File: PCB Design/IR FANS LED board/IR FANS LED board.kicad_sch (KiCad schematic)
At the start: 9 parts

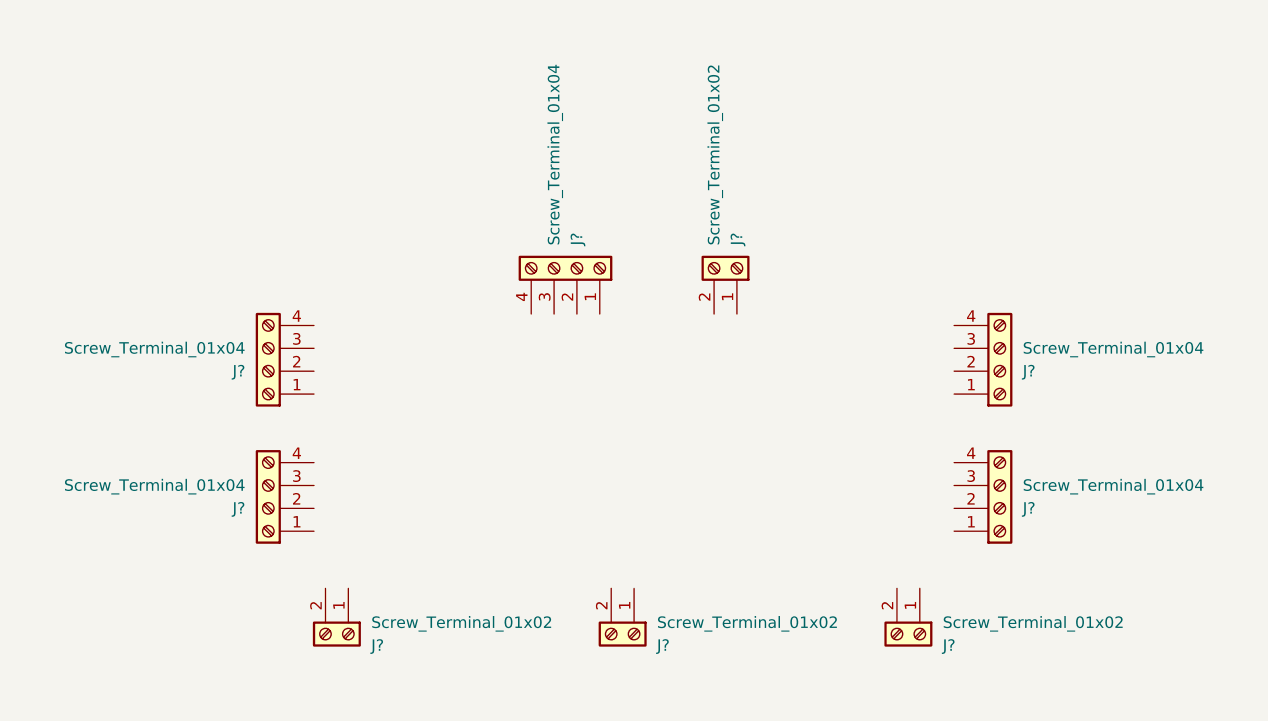
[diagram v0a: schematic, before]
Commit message: schematic now has no errors
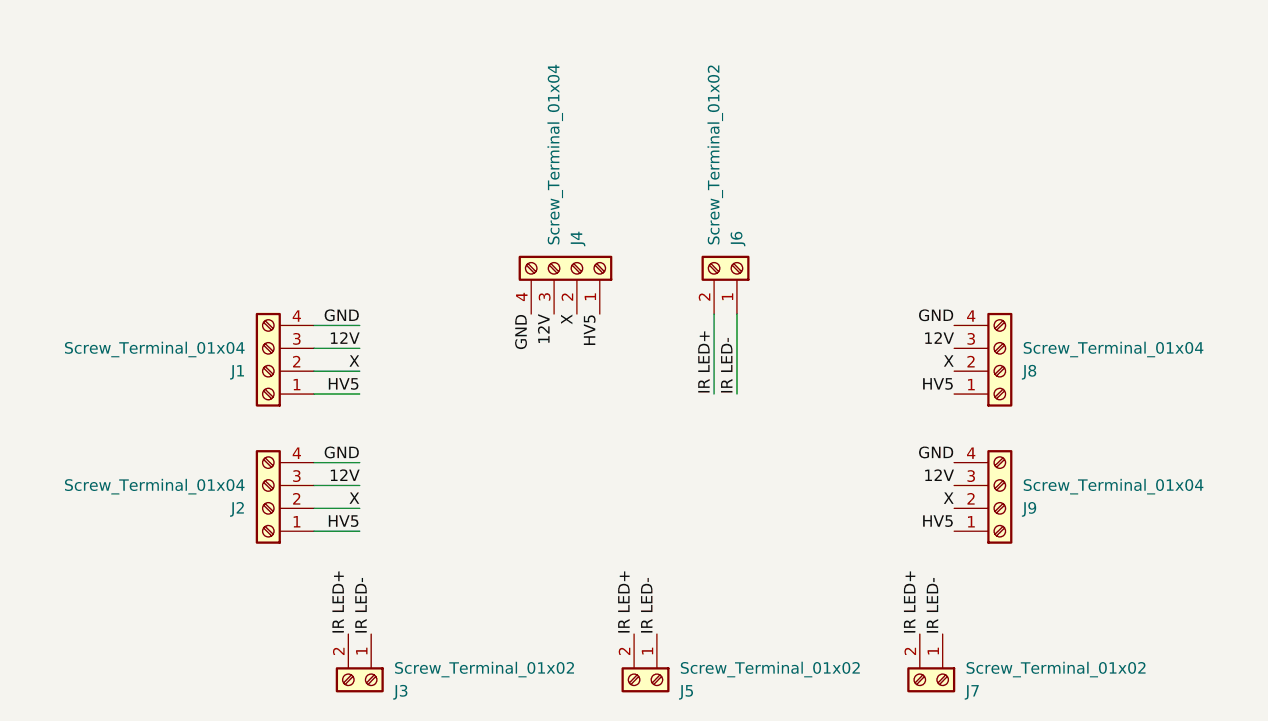
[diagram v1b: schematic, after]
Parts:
- gave numbers to parts that had none: 9
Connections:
- net HV5: now reaches J2.1 (Pin_1)
- net HV5: now also J1.1 (Pin_1), J4.1 (Pin_1), J8.1 (Pin_1), J9.1 (Pin_1)
- net X: now reaches J2.2 (Pin_2)
- net X: now also J1.2 (Pin_2), J4.2 (Pin_2), J8.2 (Pin_2), J9.2 (Pin_2)
- net 12V: now reaches J2.3 (Pin_3)
- net 12V: now also J1.3 (Pin_3), J4.3 (Pin_3), J8.3 (Pin_3), J9.3 (Pin_3)
- net GND: now reaches J2.4 (Pin_4)
- net GND: now also J1.4 (Pin_4), J4.4 (Pin_4), J8.4 (Pin_4), J9.4 (Pin_4)
- net IR LED-: now reaches J7.1 (Pin_1)
- net IR LED-: now also J3.1 (Pin_1), J5.1 (Pin_1), J6.1 (Pin_1)
- net IR LED+: now reaches J7.2 (Pin_2)
- net IR LED+: now also J3.2 (Pin_2), J5.2 (Pin_2), J6.2 (Pin_2)
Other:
- moved on the sheet: J3, J5, J7

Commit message: Labeling on components
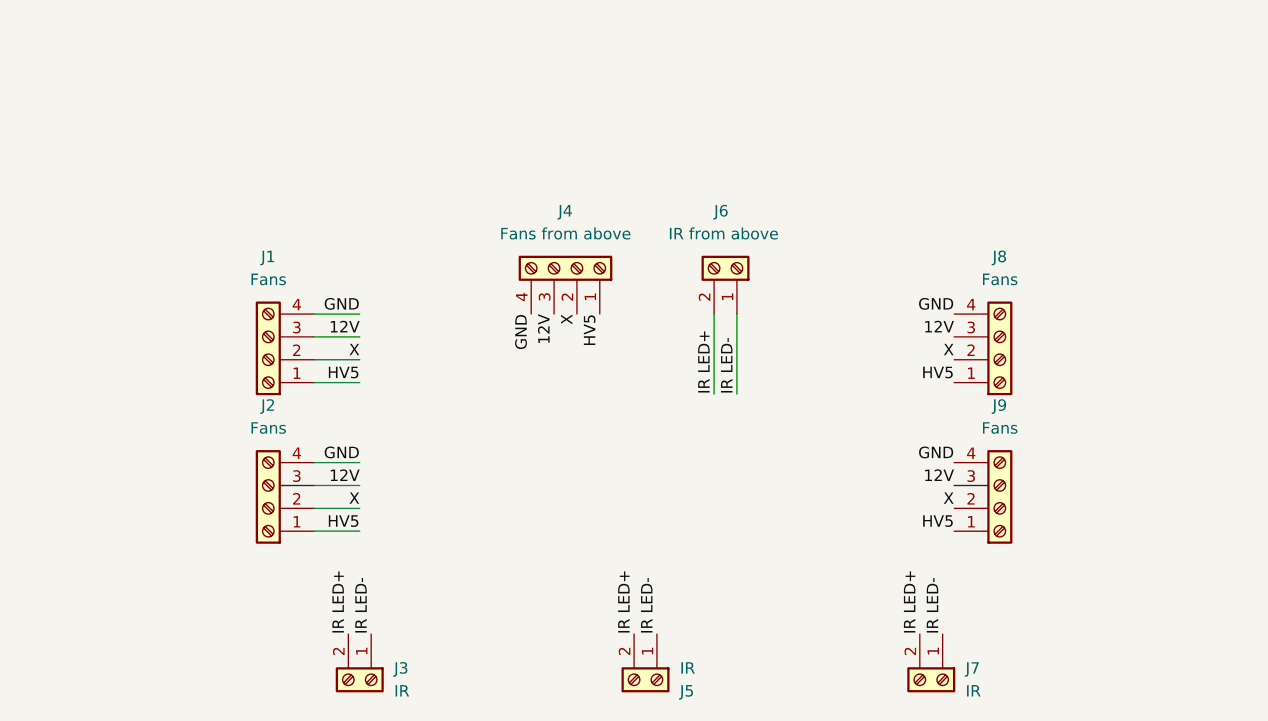
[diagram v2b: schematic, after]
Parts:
- J1, J2, J8, J9: value Screw_Terminal_01x04 -> Fans
- J3, J5, J7: value Screw_Terminal_01x02 -> IR
- J4: value Screw_Terminal_01x04 -> Fans from above
- J6: value Screw_Terminal_01x02 -> IR from above
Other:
- moved on the sheet: J1, J8

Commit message: V2 IR and RGW boards done
Main board missing button footprint
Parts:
- J3, J5, J6, J7: footprint Connector_PinHeader_2.54mm:PinHeader_1x02_P2.54mm_Vertical -> TerminalBlock:TerminalBlock_bornier-2_P5.08mm
- J4: footprint Connector_PinHeader_2.54mm:PinHeader_1x04_P2.54mm_Vertical -> TerminalBlock:TerminalBlock_bornier-4_P5.08mm
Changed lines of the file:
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@@
       (effects (font (size 1.27 1.27)) (justify left))
     )
-    (property "Footprint" "Connector_PinHeader_2.54mm:PinHeader_1x02_P2.54mm_Vertical" (id 2) (at 133.35 106.68 0)
+    (property "Footprint" "TerminalBlock:TerminalBlock_bornier-2_P5.08mm" (id 2) (at 133.35 106.68 0)
       (effects (font (size 1.27 1.27)) hide)
     )
@@
       (effects (font (size 1.27 1.27)) (justify left))
     )
-    (property "Footprint" "Connector_PinHeader_2.54mm:PinHeader_1x02_P2.54mm_Vertical" (id 2) (at 69.85 106.68 0)
+    (property "Footprint" "TerminalBlock:TerminalBlock_bornier-2_P5.08mm" (id 2) (at 69.85 106.68 0)
       (effects (font (size 1.27 1.27)) hide)
     )
@@
       (effects (font (size 1.27 1.27)) (justify left))
     )
-    (property "Footprint" "Connector_PinHeader_2.54mm:PinHeader_1x02_P2.54mm_Vertical" (id 2) (at 110.49 60.96 0)
+    (property "Footprint" "TerminalBlock:TerminalBlock_bornier-2_P5.08mm" (id 2) (at 110.49 60.96 0)
       (effects (font (size 1.27 1.27)) hide)
     )
@@
       (effects (font (size 1.27 1.27)) (justify left))
     )
-    (property "Footprint" "Connector_PinHeader_2.54mm:PinHeader_1x02_P2.54mm_Vertical" (id 2) (at 101.6 106.68 0)
+    (property "Footprint" "TerminalBlock:TerminalBlock_bornier-2_P5.08mm" (id 2) (at 101.6 106.68 0)
       (effects (font (size 1.27 1.27)) hide)
     )
@@
     (property "Reference" "J4" (id 0) (at 91.44 54.61 90))
     (property "Value" "Fans from above" (id 1) (at 91.44 57.15 90))
-    (property "Footprint" "Connector_PinHeader_2.54mm:PinHeader_1x04_P2.54mm_Vertical" (id 2) (at 92.71 60.96 0)
+    (property "Footprint" "TerminalBlock:TerminalBlock_bornier-4_P5.08mm" (id 2) (at 92.71 60.96 0)
       (effects (font (size 1.27 1.27)) hide)
     )
@@
     )
     (path "/609e8a66-54cb-40fe-9889-7eaa62dba117"
-      (reference "J3") (unit 1) (value "IR") (footprint "Connector_PinHeader_2.54mm:PinHeader_1x02_P2.54mm_Vertical")
+      (reference "J3") (unit 1) (value "IR") (footprint "TerminalBlock:TerminalBlock_bornier-2_P5.08mm")
     )
     (path "/fd479909-e292-4092-97ac-01b2689407fd"
-      (reference "J4") (unit 1) (value "Fans from above") (footprint "Connector_PinHeader_2.54mm:PinHeader_1x04_P2.54mm_Vertical")
+      (reference "J4") (unit 1) (value "Fans from above") (footprint "TerminalBlock:TerminalBlock_bornier-4_P5.08mm")
     )
     (path "/b58268f9-87ea-4c46-ab23-f79565efd06e"
-      (reference "J5") (unit 1) (value "IR") (footprint "Connector_PinHeader_2.54mm:PinHeader_1x02_P2.54mm_Vertical")
+      (reference "J5") (unit 1) (value "IR") (footprint "TerminalBlock:TerminalBlock_bornier-2_P5.08mm")
     )
     (path "/88f10c66-dda7-46b8-8caf-c98ed0e09c27"
-      (reference "J6") (unit 1) (value "IR from above") (footprint "Connector_PinHeader_2.54mm:PinHeader_1x02_P2.54mm_Vertical")
+      (reference "J6") (unit 1) (value "IR from above") (footprint "TerminalBlock:TerminalBlock_bornier-2_P5.08mm")
     )
     (path "/59271f0a-9961-4fdc-9254-d35e340b8844"
-      (reference "J7") (unit 1) (value "IR") (footprint "Connector_PinHeader_2.54mm:PinHeader_1x02_P2.54mm_Vertical")
+      (reference "J7") (unit 1) (value "IR") (footprint "TerminalBlock:TerminalBlock_bornier-2_P5.08mm")
     )
     (path "/9e3c7d3b-e05d-400a-86d2-a242affe8a13"
